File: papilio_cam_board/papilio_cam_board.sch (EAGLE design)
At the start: 3 parts

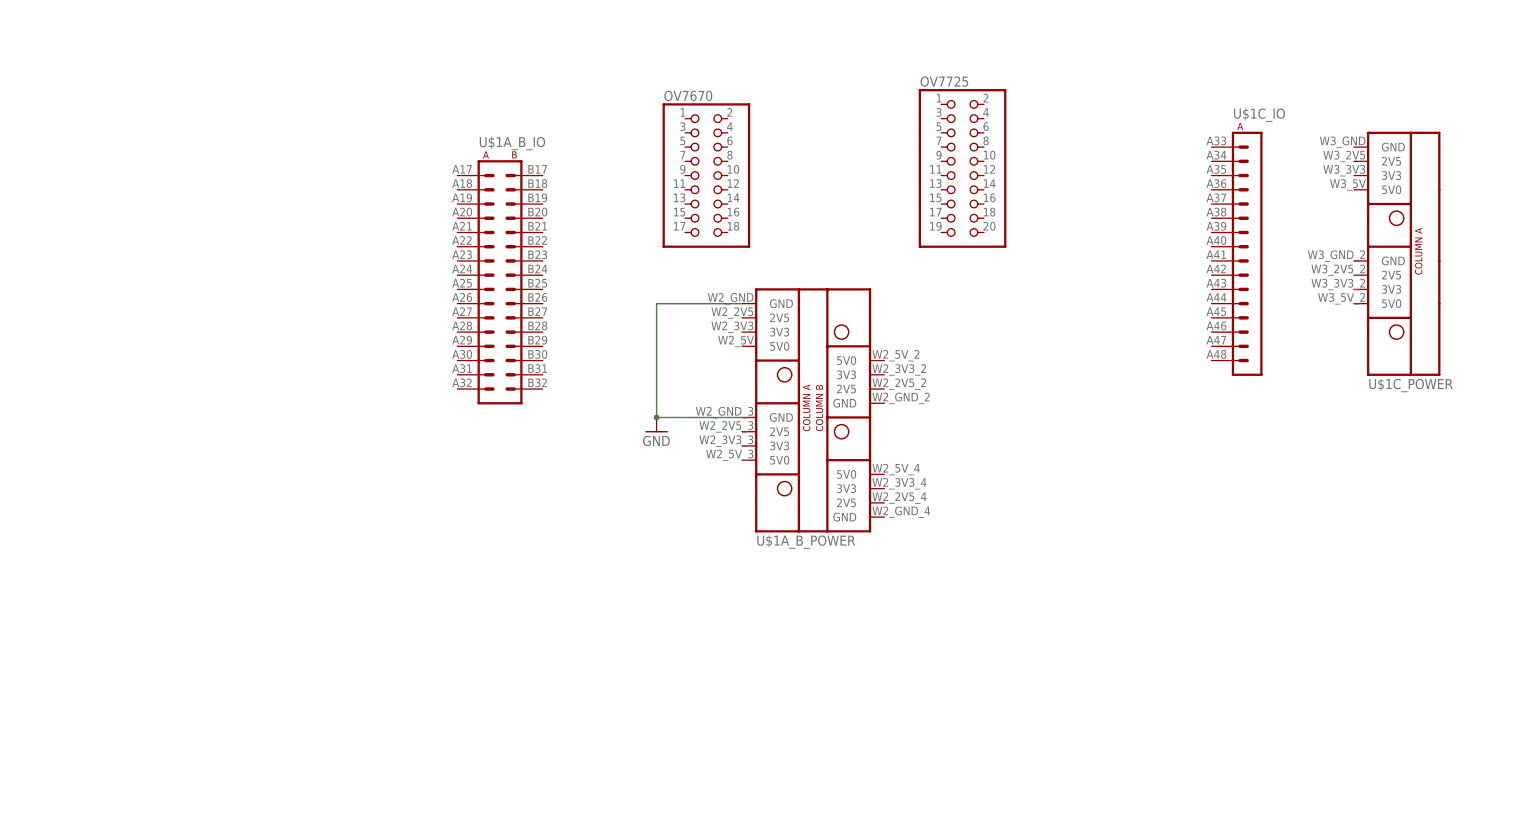
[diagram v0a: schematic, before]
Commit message: adding papilio wing to support camera sensor and other ports
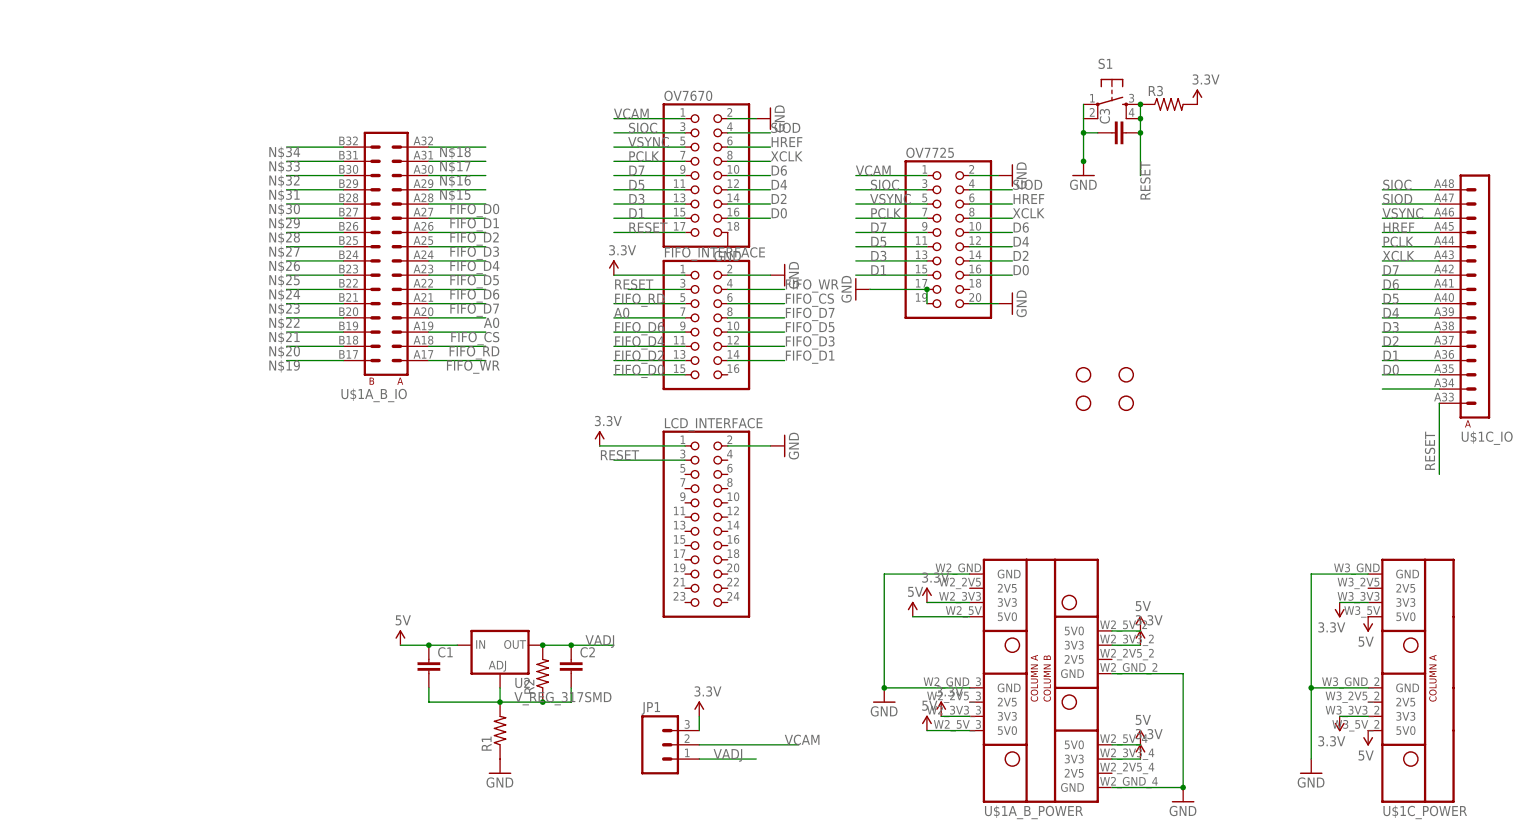
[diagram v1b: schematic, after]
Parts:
- added C1, C2, C3: (no value), SparkFun:CAP0805
- added FIFO_INTERFACE: (no value), pinhead:PINHD-2X8
- added JP1: (no value), SparkFun:M03PTH
- added JP2, JP3, JP4, JP5: STAND-OFF, SparkFun:STAND-OFF
- added LCD_INTERFACE: (no value), pinhead:PINHD-2X12
- added LOGO1: BUTTERFLY_LOGO, Papilio:BUTTERFLY_LOGO
- added R1, R2, R3: (no value), SparkFun:RESISTOR0805-RES
- added S1: (no value), SparkFun:TAC_SWITCHSMD
- added U2: V_REG_317SMD, SparkFun:V_REG_317SMD
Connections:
- new net 3.3V: FIFO_INTERFACE.1, JP1.3, LCD_INTERFACE.1, R3.2, U$1A_B_POWER.3V3@P11, U$1A_B_POWER.3V3@P14, U$1A_B_POWER.3V3@P3, U$1A_B_POWER.3V3@P6, U$1C_POWER.3V3@P3, U$1C_POWER.3V3@P7
- new net 5V: C1.1, U$1A_B_POWER.5V0@P12, U$1A_B_POWER.5V0@P13, U$1A_B_POWER.5V0@P4, U$1A_B_POWER.5V0@P5, U$1C_POWER.5V0@P4, U$1C_POWER.5V0@P8, U2.IN
- new net A0: FIFO_INTERFACE.7, U$1A_B_IO.A4
- new net D0: OV7670.16, OV7725.16, U$1C_IO.A3
- new net D1: OV7670.15, OV7725.15, U$1C_IO.A4
- new net D2: OV7670.14, OV7725.14, U$1C_IO.A5
- new net D3: OV7670.13, OV7725.13, U$1C_IO.A6
- new net D4: OV7670.12, OV7725.12, U$1C_IO.A7
- new net D5: OV7670.11, OV7725.11, U$1C_IO.A8
- new net D6: OV7670.10, OV7725.10, U$1C_IO.A9
- new net D7: OV7670.9, OV7725.9, U$1C_IO.A10
- new net FIFO_CS: FIFO_INTERFACE.6, U$1A_B_IO.A3
- new net FIFO_D0: FIFO_INTERFACE.15, U$1A_B_IO.A12
- new net FIFO_D1: FIFO_INTERFACE.14, U$1A_B_IO.A11
- new net FIFO_D2: FIFO_INTERFACE.13, U$1A_B_IO.A10
- new net FIFO_D3: FIFO_INTERFACE.12, U$1A_B_IO.A9
- new net FIFO_D4: FIFO_INTERFACE.11, U$1A_B_IO.A8
- new net FIFO_D5: FIFO_INTERFACE.10, U$1A_B_IO.A7
- new net FIFO_D6: FIFO_INTERFACE.9, U$1A_B_IO.A6
- new net FIFO_D7: FIFO_INTERFACE.8, U$1A_B_IO.A5
- new net FIFO_RD: FIFO_INTERFACE.5, U$1A_B_IO.A2
- new net FIFO_WR: FIFO_INTERFACE.4, U$1A_B_IO.A1
- new net HREF: OV7670.6, OV7725.6, U$1C_IO.A13
- new net N$1: C1.2, C2.2, R1.2, R2.1, U2.ADJ
- new net N$15: U$1A_B_IO.A13
- new net N$16: U$1A_B_IO.A14
- new net N$17: U$1A_B_IO.A15
- new net N$18: U$1A_B_IO.A16
- new net N$19: U$1A_B_IO.B1
- new net N$2: U$1C_IO.A2
- new net N$20: U$1A_B_IO.B2
- new net N$21: U$1A_B_IO.B3
- new net N$22: U$1A_B_IO.B4
- new net N$23: U$1A_B_IO.B5
- new net N$24: U$1A_B_IO.B6
- new net N$25: U$1A_B_IO.B7
- new net N$26: U$1A_B_IO.B8
- new net N$27: U$1A_B_IO.B9
- new net N$28: U$1A_B_IO.B10
- new net N$29: U$1A_B_IO.B11
- new net N$30: U$1A_B_IO.B12
- new net N$31: U$1A_B_IO.B13
- new net N$32: U$1A_B_IO.B14
- new net N$33: U$1A_B_IO.B15
- new net N$34: U$1A_B_IO.B16
- new net PCLK: OV7670.7, OV7725.7, U$1C_IO.A12
- new net RESET: C3.2, FIFO_INTERFACE.3, LCD_INTERFACE.3, OV7670.17, R3.1, S1.3, S1.4, U$1C_IO.A1
- new net SIOC: OV7670.3, OV7725.3, U$1C_IO.A16
- new net SIOD: OV7670.4, OV7725.4, U$1C_IO.A15
- new net VADJ: C2.1, JP1.1, R2.2, U2.OUT
- new net VCAM: JP1.2, OV7670.1, OV7725.1
- new net VSYNC: OV7670.5, OV7725.5, U$1C_IO.A14
- new net XCLK: OV7670.8, OV7725.8, U$1C_IO.A11
- net GND: now also C3.1, FIFO_INTERFACE.2, LCD_INTERFACE.2, OV7670.18, OV7670.2, OV7725.17, OV7725.19, OV7725.2, OV7725.20, R1.1, S1.1, S1.2, U$1A_B_POWER.GND@P16, U$1A_B_POWER.GND@P8, U$1C_POWER.GND@P1, U$1C_POWER.GND@P5
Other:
- moved on the sheet: OV7725, U$1A_B_IO, U$1A_B_POWER, U$1C_IO, U$1C_POWER

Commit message: 
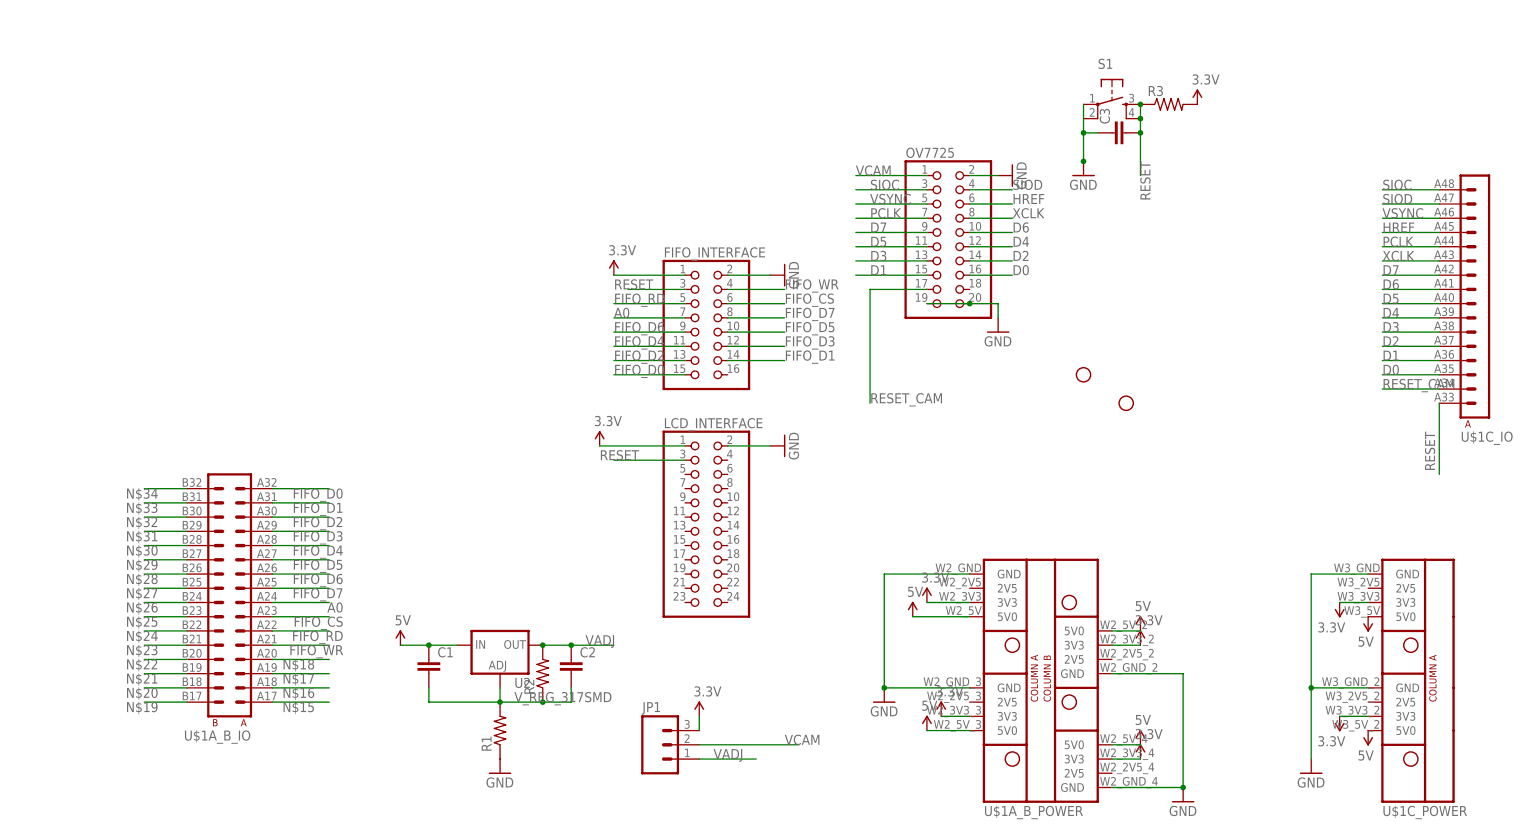
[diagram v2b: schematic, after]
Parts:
- removed JP3, JP4: STAND-OFF, SparkFun:STAND-OFF
- removed OV7670: (no value), pinhead:PINHD-2X9
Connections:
- removed net N$2: U$1C_IO.A2
- new net RESET_CAM: OV7725.17, U$1C_IO.A2
- net A0: now also U$1A_B_IO.A8; no longer U$1A_B_IO.A4
- net D0: no longer OV7670.16
- net D1: no longer OV7670.15
- net D2: no longer OV7670.14
- net D3: no longer OV7670.13
- net D4: no longer OV7670.12
- net D5: no longer OV7670.11
- net D6: no longer OV7670.10
- net D7: no longer OV7670.9
- net FIFO_CS: now also U$1A_B_IO.A7; no longer U$1A_B_IO.A3
- net FIFO_D0: now also U$1A_B_IO.A16; no longer U$1A_B_IO.A12
- net FIFO_D1: now also U$1A_B_IO.A15; no longer U$1A_B_IO.A11
- net FIFO_D2: now also U$1A_B_IO.A14; no longer U$1A_B_IO.A10
- net FIFO_D3: now also U$1A_B_IO.A13; no longer U$1A_B_IO.A9
- net FIFO_D4: now also U$1A_B_IO.A12; no longer U$1A_B_IO.A8
- net FIFO_D5: now also U$1A_B_IO.A11; no longer U$1A_B_IO.A7
- net FIFO_D6: now also U$1A_B_IO.A10; no longer U$1A_B_IO.A6
- net FIFO_D7: now also U$1A_B_IO.A9; no longer U$1A_B_IO.A5
- net FIFO_RD: now also U$1A_B_IO.A6; no longer U$1A_B_IO.A2
- net FIFO_WR: now also U$1A_B_IO.A5; no longer U$1A_B_IO.A1
- net GND: no longer OV7670.18, OV7670.2, OV7725.17
- net HREF: no longer OV7670.6
- net N$15: now also U$1A_B_IO.A1; no longer U$1A_B_IO.A13
- net N$16: now also U$1A_B_IO.A2; no longer U$1A_B_IO.A14
- net N$17: now also U$1A_B_IO.A3; no longer U$1A_B_IO.A15
- net N$18: now also U$1A_B_IO.A4; no longer U$1A_B_IO.A16
- net PCLK: no longer OV7670.7
- net RESET: no longer OV7670.17
- net SIOC: no longer OV7670.3
- net SIOD: no longer OV7670.4
- net VCAM: no longer OV7670.1
- net VSYNC: no longer OV7670.5
- net XCLK: no longer OV7670.8
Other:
- moved on the sheet: U$1A_B_IO

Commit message: 
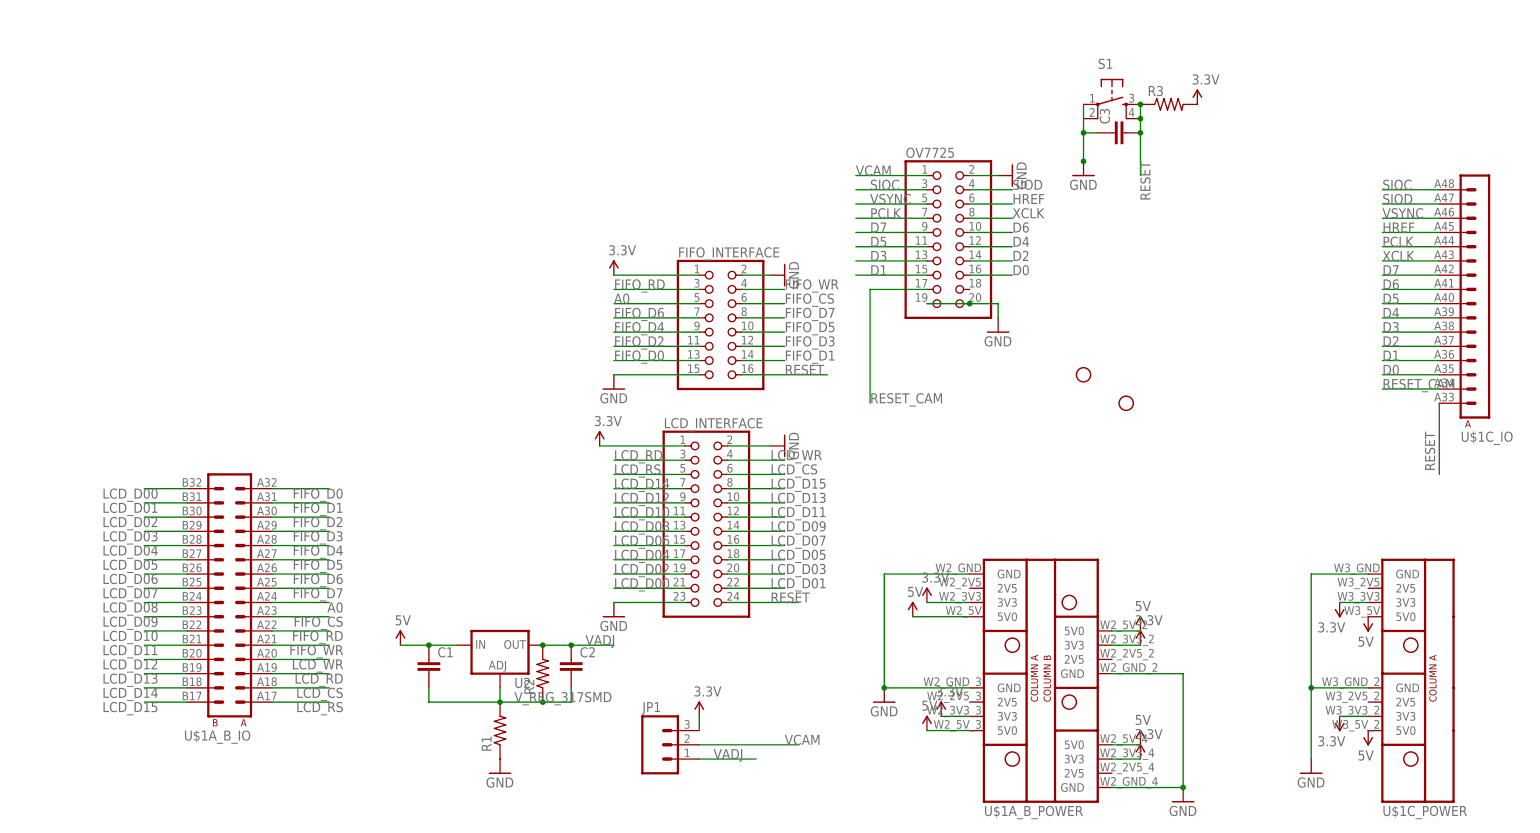
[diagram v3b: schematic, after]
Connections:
- removed net N$15: U$1A_B_IO.A1
- removed net N$16: U$1A_B_IO.A2
- removed net N$17: U$1A_B_IO.A3
- removed net N$18: U$1A_B_IO.A4
- removed net N$19: U$1A_B_IO.B1
- removed net N$20: U$1A_B_IO.B2
- removed net N$21: U$1A_B_IO.B3
- removed net N$22: U$1A_B_IO.B4
- removed net N$23: U$1A_B_IO.B5
- removed net N$24: U$1A_B_IO.B6
- removed net N$25: U$1A_B_IO.B7
- removed net N$26: U$1A_B_IO.B8
- removed net N$27: U$1A_B_IO.B9
- removed net N$28: U$1A_B_IO.B10
- removed net N$29: U$1A_B_IO.B11
- removed net N$30: U$1A_B_IO.B12
- removed net N$31: U$1A_B_IO.B13
- removed net N$32: U$1A_B_IO.B14
- removed net N$33: U$1A_B_IO.B15
- removed net N$34: U$1A_B_IO.B16
- new net LCD_CS: LCD_INTERFACE.6, U$1A_B_IO.A2
- new net LCD_D00: LCD_INTERFACE.21, U$1A_B_IO.B16
- new net LCD_D01: LCD_INTERFACE.22, U$1A_B_IO.B15
- new net LCD_D02: LCD_INTERFACE.19, U$1A_B_IO.B14
- new net LCD_D03: LCD_INTERFACE.20, U$1A_B_IO.B13
- new net LCD_D04: LCD_INTERFACE.17, U$1A_B_IO.B12
- new net LCD_D05: LCD_INTERFACE.18, U$1A_B_IO.B11
- new net LCD_D06: LCD_INTERFACE.15, U$1A_B_IO.B10
- new net LCD_D07: LCD_INTERFACE.16, U$1A_B_IO.B9
- new net LCD_D08: LCD_INTERFACE.13, U$1A_B_IO.B8
- new net LCD_D09: LCD_INTERFACE.14, U$1A_B_IO.B7
- new net LCD_D10: LCD_INTERFACE.11, U$1A_B_IO.B6
- new net LCD_D11: LCD_INTERFACE.12, U$1A_B_IO.B5
- new net LCD_D12: LCD_INTERFACE.9, U$1A_B_IO.B4
- new net LCD_D13: LCD_INTERFACE.10, U$1A_B_IO.B3
- new net LCD_D14: LCD_INTERFACE.7, U$1A_B_IO.B2
- new net LCD_D15: LCD_INTERFACE.8, U$1A_B_IO.B1
- new net LCD_RD: LCD_INTERFACE.3, U$1A_B_IO.A3
- new net LCD_RS: LCD_INTERFACE.5, U$1A_B_IO.A1
- new net LCD_WR: LCD_INTERFACE.4, U$1A_B_IO.A4
- net A0: now also FIFO_INTERFACE.5; no longer FIFO_INTERFACE.7
- net FIFO_D0: now also FIFO_INTERFACE.13; no longer FIFO_INTERFACE.15
- net FIFO_D2: now also FIFO_INTERFACE.11; no longer FIFO_INTERFACE.13
- net FIFO_D4: now also FIFO_INTERFACE.9; no longer FIFO_INTERFACE.11
- net FIFO_D6: now also FIFO_INTERFACE.7; no longer FIFO_INTERFACE.9
- net FIFO_RD: now also FIFO_INTERFACE.3; no longer FIFO_INTERFACE.5
- net GND: now also FIFO_INTERFACE.15, LCD_INTERFACE.23
- net RESET: now also FIFO_INTERFACE.16, LCD_INTERFACE.24; no longer FIFO_INTERFACE.3, LCD_INTERFACE.3
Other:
- moved on the sheet: FIFO_INTERFACE

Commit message: adding papilio wing to support camera sensor and other ports
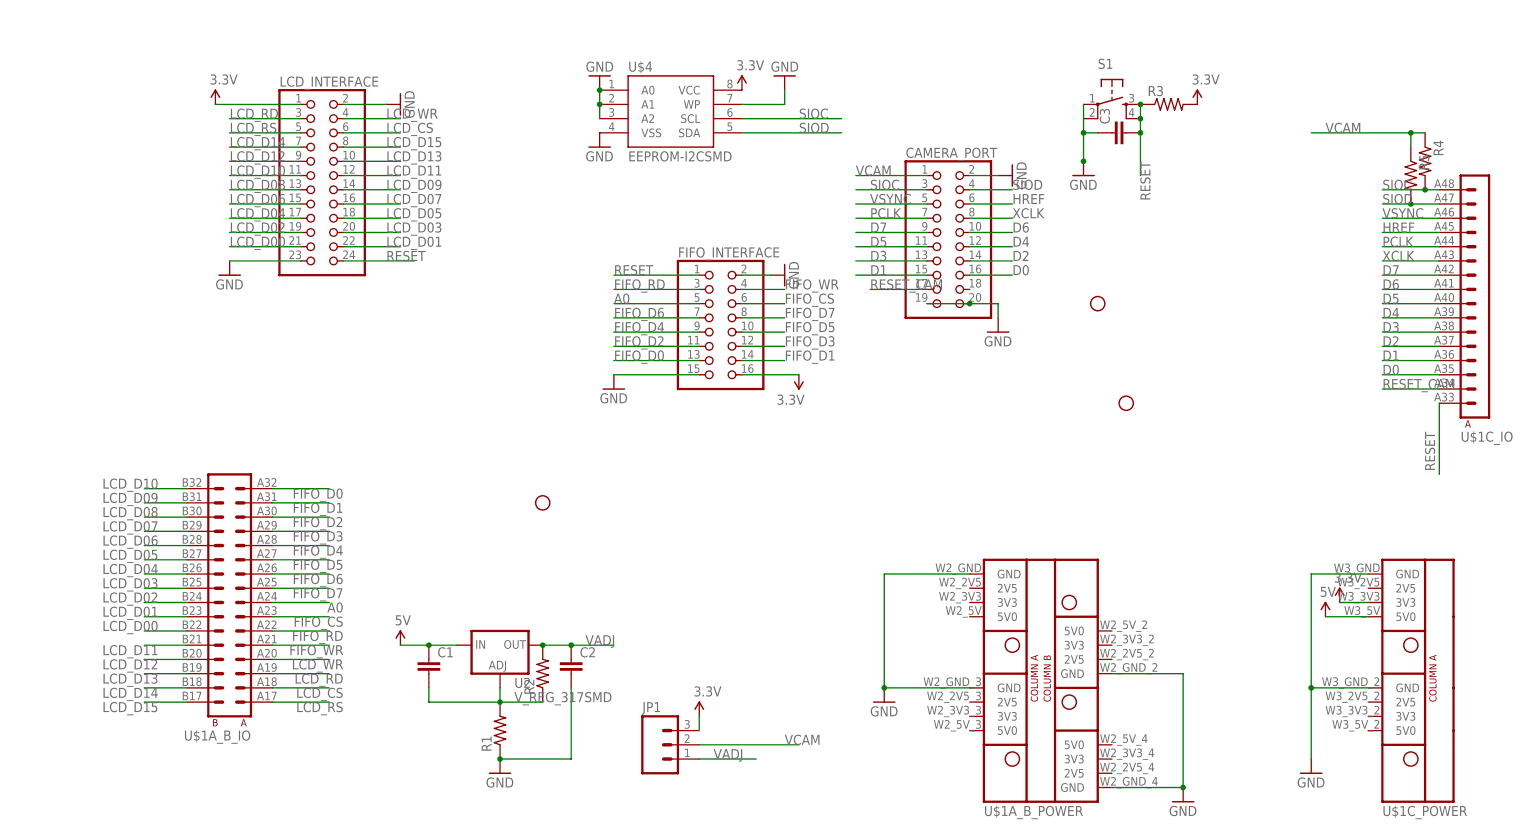
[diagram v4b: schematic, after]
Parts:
- added JP7: STAND-OFF, SparkFun:STAND-OFF
- added R4, R5: (no value), SparkFun:RESISTOR0805-RES
- added U$4: EEPROM-I2CSMD, SparkFun:EEPROM-I2CSMD
- renumbered OV7725 to CAMERA_PORT
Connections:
- net 3.3V: now also FIFO_INTERFACE.16, U$4.VCC; no longer FIFO_INTERFACE.1, U$1A_B_POWER.3V3@P11, U$1A_B_POWER.3V3@P14, U$1A_B_POWER.3V3@P3, U$1A_B_POWER.3V3@P6, U$1C_POWER.3V3@P7
- net 5V: no longer U$1A_B_POWER.5V0@P12, U$1A_B_POWER.5V0@P13, U$1A_B_POWER.5V0@P4, U$1A_B_POWER.5V0@P5, U$1C_POWER.5V0@P8
- net GND: now also C2.2, U$4.A0, U$4.A1, U$4.A2, U$4.VSS, U$4.WP
- net LCD_D00: now also U$1A_B_IO.B6; no longer U$1A_B_IO.B16
- net LCD_D01: now also U$1A_B_IO.B7; no longer U$1A_B_IO.B15
- net LCD_D02: now also U$1A_B_IO.B8; no longer U$1A_B_IO.B14
- net LCD_D03: now also U$1A_B_IO.B9; no longer U$1A_B_IO.B13
- net LCD_D04: now also U$1A_B_IO.B10; no longer U$1A_B_IO.B12
- net LCD_D06: now also U$1A_B_IO.B12; no longer U$1A_B_IO.B10
- net LCD_D07: now also U$1A_B_IO.B13; no longer U$1A_B_IO.B9
- net LCD_D08: now also U$1A_B_IO.B14; no longer U$1A_B_IO.B8
- net LCD_D09: now also U$1A_B_IO.B15; no longer U$1A_B_IO.B7
- net LCD_D10: now also U$1A_B_IO.B16; no longer U$1A_B_IO.B6
- net N$1: no longer C2.2
- net RESET: now also FIFO_INTERFACE.1; no longer FIFO_INTERFACE.16
- net SIOC: now also R4.2, U$4.SCL
- net SIOD: now also R5.2, U$4.SDA
- net VCAM: now also R4.1, R5.1
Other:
- moved on the sheet: LCD_INTERFACE
